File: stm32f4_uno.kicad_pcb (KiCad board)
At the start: 2 copper layers, 68.6 x 53.3 mm, 73 parts, among them J101 STM32 GPIO, J102 Digital/PWM, J103 STM32 GPIO, J104 STM32 GPIO, J105 STM32 GPIO, J106 Power, J107 Ethernet, J108 STM32 GPIO, J109 Digital/PWM, J110 Analog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

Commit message: #10 Wrong text on pin 3 (J102)
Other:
- board text added: "V_{REF+}"

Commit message: #15 Add all pin sockets
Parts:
- added J111: Conn_01x04, Connector_PinSocket_2.54mm:PinSocket_1x04_P2.54mm_Vertical, F.Cu at (118.8, 58.5)
- moved G*** 6.11 mm to (134.0, 59.9)
- renumbered J111 to J1
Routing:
- net /PE12: track 28.9 -> 29.8 mm

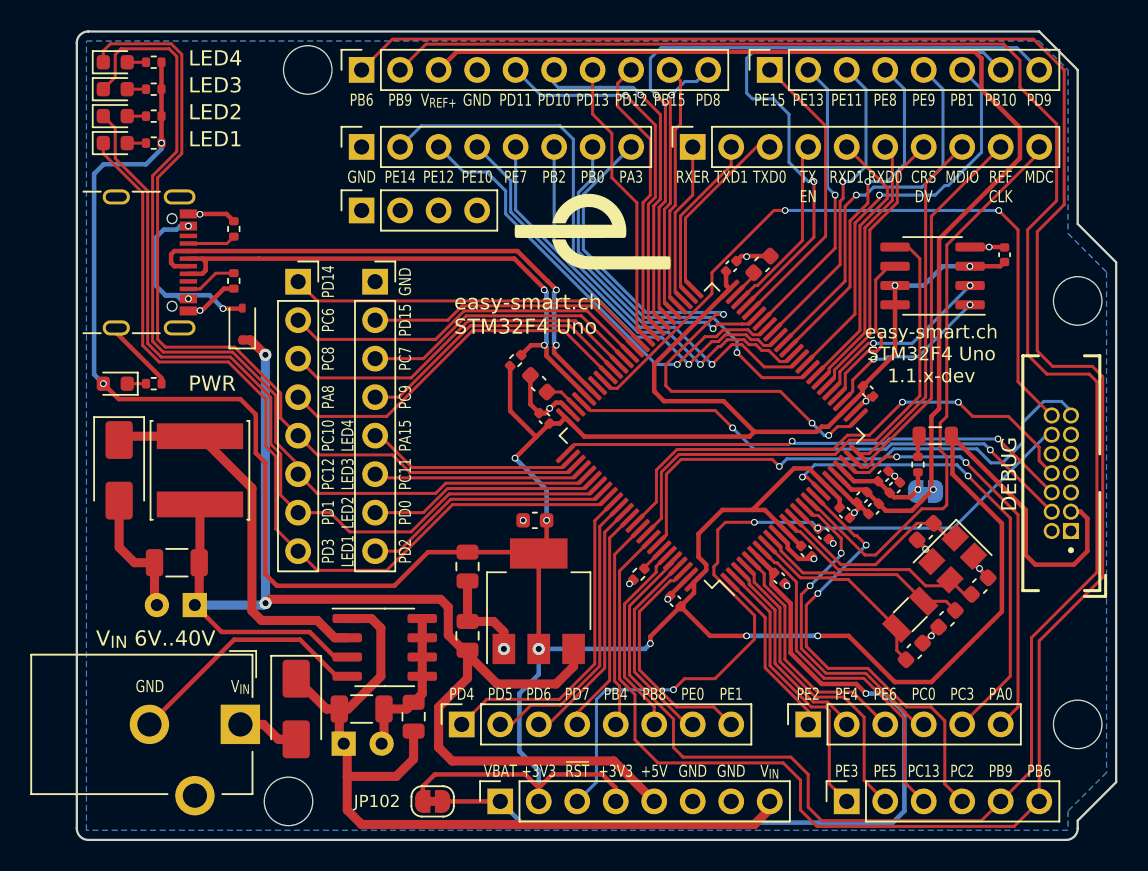
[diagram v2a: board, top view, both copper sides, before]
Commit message: #14 Add optional capacitor for RTC operation
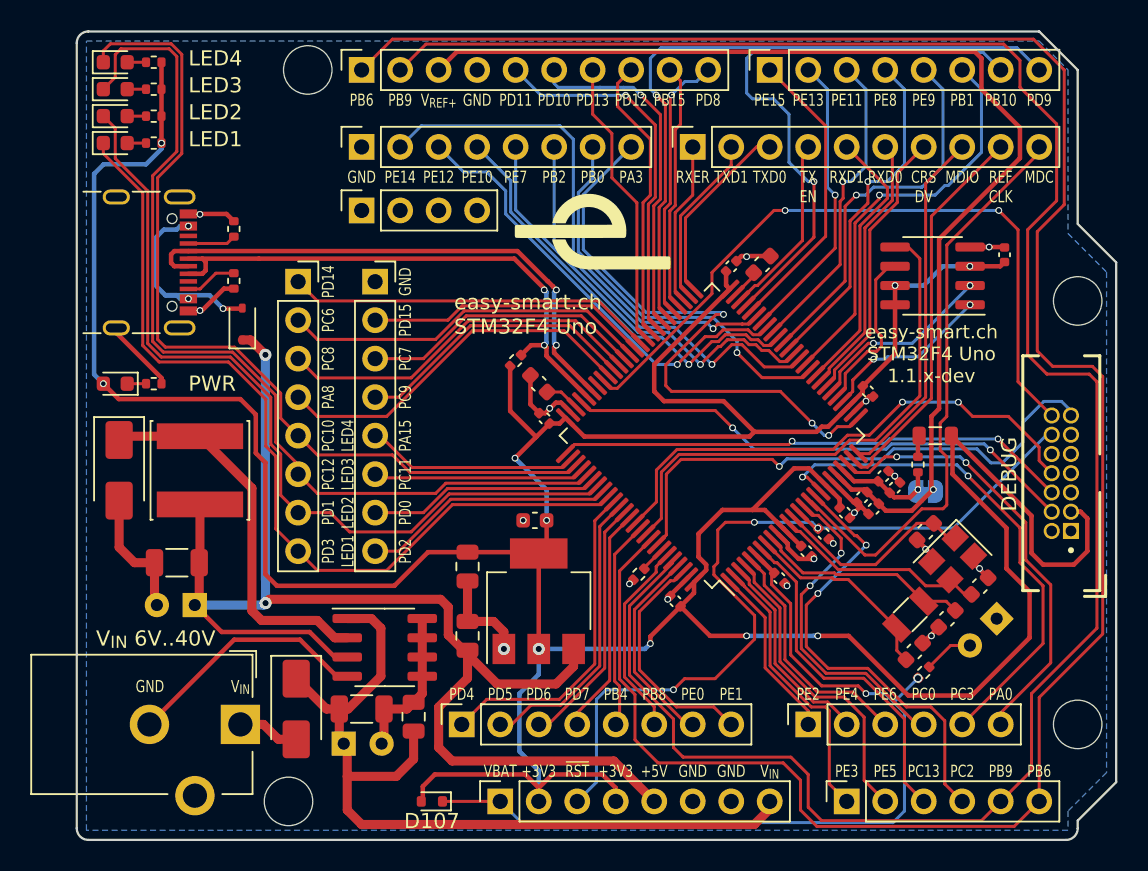
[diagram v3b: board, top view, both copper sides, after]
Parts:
- removed JP102: Jumper_2_Bridged, Jumper:SolderJumper-2_P1.3mm_Bridged_RoundedPad1.0x1.5mm
- added C120: ?, Capacitor_THT:CP_Radial_D6.3mm_P2.50mm, B.Cu at (160.7, 85.4)
- added D107: 1N4148WT, Diode_SMD:D_SOD-523, F.Cu at (123.4, 97.5)
- added R107: 100, Resistor_SMD:R_0402_1005Metric, F.Cu at (155.9, 89.0)
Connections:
- J111 pad 1: (no net) -> unconnected-(J111-Pin_1-Pad1)
- J111 pad 2: (no net) -> unconnected-(J111-Pin_2-Pad2)
- J111 pad 3: (no net) -> unconnected-(J111-Pin_3-Pad3)
- J111 pad 4: (no net) -> unconnected-(J111-Pin_4-Pad4)
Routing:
- net +3V3: track 262.8 -> 266.8 mm
- net Net-(C120-Pad2): track 0.00 -> 3.27 mm
- net /VBAT: track 56.0 -> 58.3 mm, vias 1 -> 2
- net /PC3: track 32.0 -> 33.8 mm
- net /PA0: track 27.8 -> 29.6 mm

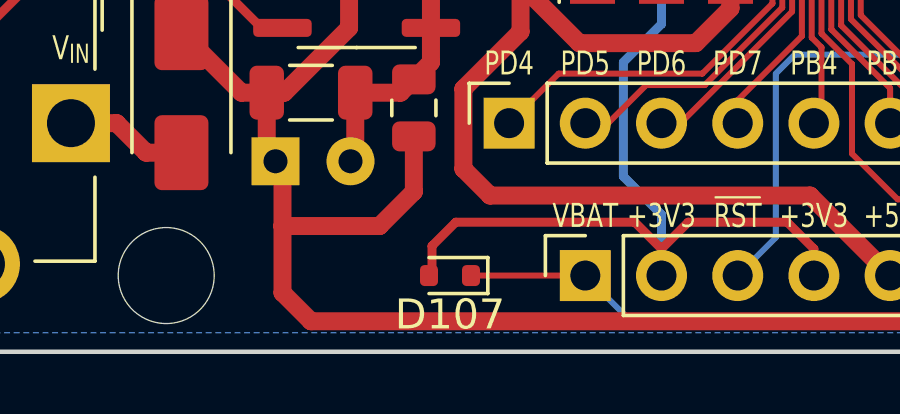
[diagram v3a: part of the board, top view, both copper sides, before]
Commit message: #16 Silkscreen texts
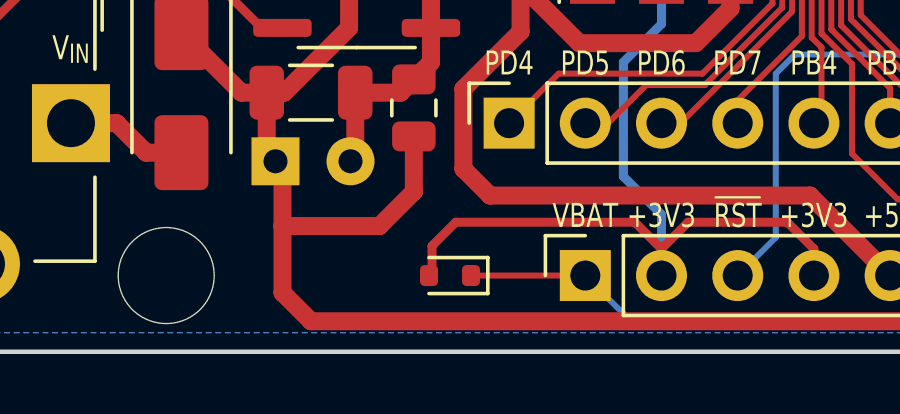
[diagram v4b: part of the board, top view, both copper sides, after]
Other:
- board text added: "(5V)"
- board text added: "(RTC)"
- board text added: "(VREF)"
- board text added: "(V_{IN})"
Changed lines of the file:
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@@
 		(tags "Diode SOD523")
 		(property "Reference" "D107"
-			(at 0 -1.3 360)
+			(at 0 -1.3 0)
 			(layer "F.SilkS")
+			(hide yes)
 			(effects
 				(font
@@
 		)
 		(property "Value" "1N4148WT"
-			(at 0 1.4 360)
+			(at 0 1.4 0)
 			(layer "F.Fab")
 			(effects
@@
 		)
 		(fp_text user "${REFERENCE}"
-			(at 0 -1.3 360)
+			(at 0 -1.3 0)
 			(layer "F.Fab")
 			(effects
@@
 		)
 		(fp_text user "${REFERENCE}"
-			(at 0 3.81 360)
+			(at 0 3.81 0)
 			(layer "F.Fab")
 			(effects
@@
 		)
 	)
+	(gr_text "(RTC)"
+		(at 154.7368 85.9028 45)
+		(layer "B.SilkS")
+		(effects
+			(font
+				(size 0.8 0.6)
+				(thickness 0.08)
+			)
+			(justify bottom mirror)
+		)
+	)
 	(gr_text "V_{REF+}"
 		(at 123.8758 50.7238 0)
@@
 		)
 	)
+	(gr_text "(V_{IN})"
+		(at 115.6208 89.8398 0)
+		(layer "B.SilkS")
+		(effects
+			(font
+				(size 0.8 0.6)
+				(thickness 0.08)
+			)
+			(justify bottom mirror)
+		)
+	)
 	(gr_text "GND"
 		(at 104.8258 90.3478 0)
@@
 		)
 	)
+	(gr_text "(5V)"
+		(at 103.5558 80.5688 0)
+		(layer "B.SilkS")
+		(effects
+			(font
+				(size 0.8 0.6)
+				(thickness 0.08)
+			)
+			(justify bottom mirror)
+		)
+	)
 	(gr_text "PB6"
 		(at 118.7958 50.7238 0)
@@
 		)
 	)
+	(gr_text "(VREF)"
+		(at 152.4508 75.7428 0)
+		(layer "B.SilkS")
+		(effects
+			(font
+				(size 0.8 0.6)
+				(thickness 0.08)
+			)
+			(justify bottom mirror)
+		)
+	)
